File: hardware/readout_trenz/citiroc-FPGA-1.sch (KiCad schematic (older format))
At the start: 17 parts

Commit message: Trenz Module Work in Progress
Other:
- note added: "Replace FPGA with trenz"
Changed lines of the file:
@@
 $Descr A4 11693 8268
 encoding utf-8
-Sheet 11 12
+Sheet 11 13
 Title ""
 Date ""
@@
 	1    0    0    -1
 $EndComp
+Text Notes 4250 1000 0    197  ~ 0
+Replace FPGA with trenz
 $EndSCHEMATC

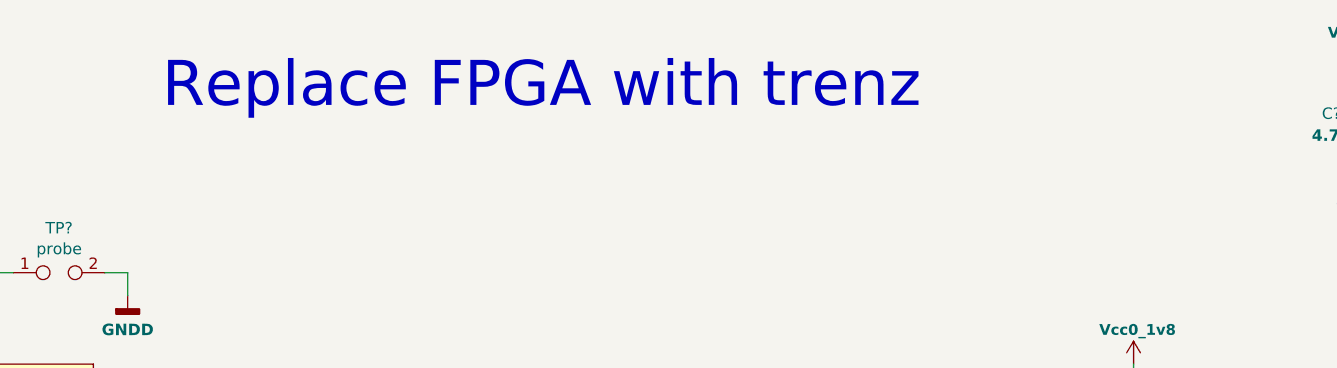
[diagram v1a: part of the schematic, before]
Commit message: Readout Trenz edited
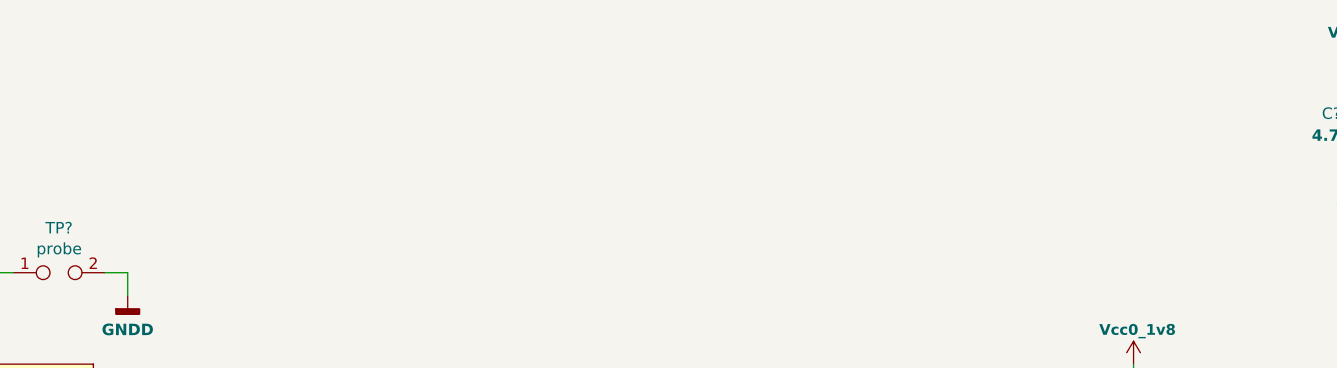
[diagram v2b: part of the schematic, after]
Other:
- note removed: "Replace FPGA with trenz"
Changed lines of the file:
@@
 $Descr A4 11693 8268
 encoding utf-8
-Sheet 11 13
+Sheet 11 20
 Title ""
 Date ""
@@
 AR Path="/605DF89A/606347B4" Ref="U?"  Part="2"
 AR Path="/606347B4" Ref="U?"  Part="2"
+AR Path="/60C32D5A/606347B4" Ref="U?"  Part="2"
 F 0 "U?" H 3375 -2123 50  0000 C CNN
 F 1 "CITIROC1A" H 3375 -2214 50  0000 C CNN
@@
 AR Path="/60548503/606347BA" Ref="U?"  Part="8"
 AR Path="/605DF89A/606347BA" Ref="U?"  Part="8"
+AR Path="/60C32D5A/606347BA" Ref="U?"  Part="8"
 F 0 "U?" H 8175 -1423 50  0000 C CNN
 F 1 "CITIROC1A" H 8175 -1514 50  0000 C CNN
@@
 AR Path="/60548503/606347C0" Ref="C?"  Part="1"
 AR Path="/605DF89A/606347C0" Ref="C?"  Part="1"
+AR Path="/60C32D5A/606347C0" Ref="C?"  Part="1"
 F 0 "C?" H 9842 1096 50  0000 L CNN
 F 1 "47u" H 9800 1000 50  0000 L CNB
@@
 AR Path="/60548503/606347C6" Ref="C?"  Part="1"
 AR Path="/605DF89A/606347C6" Ref="C?"  Part="1"
+AR Path="/60C32D5A/606347C6" Ref="C?"  Part="1"
 F 0 "C?" H 10142 1096 50  0000 L CNN
 F 1 "4.7u" H 10100 1000 50  0000 L CNB
@@
 AR Path="/60548503/606347CC" Ref="C?"  Part="1"
 AR Path="/605DF89A/606347CC" Ref="C?"  Part="1"
+AR Path="/60C32D5A/606347CC" Ref="C?"  Part="1"
 F 0 "C?" H 9592 1096 50  0000 L CNN
 F 1 "4.7u" H 9550 1000 50  0000 L CNB
@@
 AR Path="/60548503/606347D2" Ref="C?"  Part="1"
 AR Path="/605DF89A/606347D2" Ref="C?"  Part="1"
+AR Path="/60C32D5A/606347D2" Ref="C?"  Part="1"
 F 0 "C?" H 11150 1100 50  0000 L CNN
 F 1 ".47u" H 11100 1000 50  0000 L CNB
@@
 AR Path="/60548503/606347D8" Ref="C?"  Part="1"
 AR Path="/605DF89A/606347D8" Ref="C?"  Part="1"
+AR Path="/60C32D5A/606347D8" Ref="C?"  Part="1"
 F 0 "C?" H 10892 1096 50  0000 L CNN
 F 1 ".47u" H 10850 1000 50  0000 L CNB
@@
 AR Path="/60548503/606347DE" Ref="C?"  Part="1"
 AR Path="/605DF89A/606347DE" Ref="C?"  Part="1"
+AR Path="/60C32D5A/606347DE" Ref="C?"  Part="1"
 F 0 "C?" H 10642 1096 50  0000 L CNN
 F 1 ".47u" H 10600 1000 50  0000 L CNB
@@
 AR Path="/60548503/606347E4" Ref="C?"  Part="1"
 AR Path="/605DF89A/606347E4" Ref="C?"  Part="1"
+AR Path="/60C32D5A/606347E4" Ref="C?"  Part="1"
 F 0 "C?" H 10392 1096 50  0000 L CNN
 F 1 ".47u" H 10350 1000 50  0000 L CNB
@@
 AR Path="/60548503/606347EA" Ref="#PWR?"  Part="1"
 AR Path="/605DF89A/606347EA" Ref="#PWR?"  Part="1"
+AR Path="/60C32D5A/606347EA" Ref="#PWR?"  Part="1"
 F 0 "#PWR?" H 9500 1000 50  0001 C CNN
 F 1 "GNDD" H 9500 1100 50  0000 C CNB
@@
 U 1 1 608CECB3
 P 2350 2900
+AR Path="/605DF89A/608CECB3" Ref="R?"  Part="1"
+AR Path="/60C32D5A/608CECB3" Ref="R?"  Part="1"
 F 0 "R?" V 2400 3000 50  0000 L CNN
 F 1 "100" V 2350 2800 50  0000 L CNN
@@
 U 1 1 60D6A41E
 P 3800 1700
+AR Path="/605DF89A/60D6A41E" Ref="TP?"  Part="1"
+AR Path="/60C32D5A/60D6A41E" Ref="TP?"  Part="1"
 F 0 "TP?" H 3800 1895 50  0000 C CNN
 F 1 "probe" H 3800 1804 50  0000 C CNN
@@
 AR Path="/60548503/60D79EC4" Ref="#PWR?"  Part="1"
 AR Path="/605DF89A/60D79EC4" Ref="#PWR?"  Part="1"
+AR Path="/60C32D5A/60D79EC4" Ref="#PWR?"  Part="1"
 F 0 "#PWR?" H 4100 1550 50  0001 C CNN
 F 1 "GNDD" H 4100 1650 50  0000 C CNB
@@
 U 1 1 608D2690
 P 2350 2600
+AR Path="/605DF89A/608D2690" Ref="R?"  Part="1"
+AR Path="/60C32D5A/608D2690" Ref="R?"  Part="1"
 F 0 "R?" V 2400 2700 50  0000 L CNN
 F 1 "100" V 2350 2500 50  0000 L CNN
@@
 U 1 1 60CED0B7
 P 5000 5650
+AR Path="/605DF89A/60CED0B7" Ref="R?"  Part="1"
+AR Path="/60C32D5A/60CED0B7" Ref="R?"  Part="1"
 F 0 "R?" H 5070 5696 50  0000 L CNN
 F 1 "1k" V 5000 5600 50  0000 L CNN
@@
 U 1 1 60CED89A
 P 5100 5650
+AR Path="/605DF89A/60CED89A" Ref="R?"  Part="1"
+AR Path="/60C32D5A/60CED89A" Ref="R?"  Part="1"
 F 0 "R?" H 5170 5696 50  0000 L CNN
 F 1 "1k" V 5100 5600 50  0000 L CNN
@@
 U 1 1 60E0098C
 P 5000 5300
+AR Path="/605DF89A/60E0098C" Ref="U?"  Part="1"
+AR Path="/60C32D5A/60E0098C" Ref="U?"  Part="1"
 F 0 "U?" H 5000 5300 79  0001 C CNN
 F 1 "Vcc0_1v8" H 4850 5350 47  0000 L CNB
@@
 U 1 1 60E0A350
 P 8500 2000
+AR Path="/605DF89A/60E0A350" Ref="U?"  Part="1"
+AR Path="/60C32D5A/60E0A350" Ref="U?"  Part="1"
 F 0 "U?" H 8500 2000 79  0001 C CNN
 F 1 "Vcc0_1v8" H 8350 2050 47  0000 L CNB
@@
 U 1 1 60E13D1D
 P 9500 700
+AR Path="/605DF89A/60E13D1D" Ref="U?"  Part="1"
+AR Path="/60C32D5A/60E13D1D" Ref="U?"  Part="1"
 F 0 "U?" H 9500 700 79  0001 C CNN
 F 1 "Vcc0_1v8" H 9350 750 47  0000 L CNB
@@
 	1    0    0    -1
 $EndComp
-Text Notes 4250 1000 0    197  ~ 0
-Replace FPGA with trenz
 $EndSCHEMATC

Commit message: Readout Trenz in progress
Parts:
- removed C?: .47u, symbol readout_trenz-rescue:C_Small-Device
- removed R? (x2): 100, symbol readout_trenz-rescue:R-Device
- removed R? (x2): 1k, symbol readout_trenz-rescue:R-Device
- removed U? (x3): Vcc0_1v8, symbol readout:VccAux
- added C?: .47u, symbol readout_trenz-rescue:C_Small-Device
- added R? (x2): 100, symbol readout_trenz-rescue:R-Device
- added R? (x2): 1k, symbol readout_trenz-rescue:R-Device
- added U? (x3): Vcc0_1v8, symbol readout:VccAux
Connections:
- net GNDD: now also C?.2
- net NOR32T_oc_1: now also R?.2
- net NOR32_oc_1: now also R?.2
- net Raz_Chn_p1: now also R?.2
- net Raz_chn_n1: now also R?.1
- net VCC: now also C?.1, R?.1, R?.1, U?.1 (VCC), U?.1 (VCC), U?.1 (VCC)
- net Val_Ext_n1: now also R?.1
- net Val_Ext_p1: now also R?.2
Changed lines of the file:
@@
 $Descr A4 11693 8268
 encoding utf-8
-Sheet 11 20
+Sheet 12 20
 Title ""
 Date ""
@@
 $Comp
 L readout_trenz-rescue:C_Small-Device C?
-U 1 1 606347DE
+U 1 1 60C0A1D8
 P 10550 1050
-AR Path="/605605C8/606347DE" Ref="C?"  Part="1"
-AR Path="/60548503/606347DE" Ref="C?"  Part="1"
-AR Path="/605DF89A/606347DE" Ref="C?"  Part="1"
-AR Path="/60C32D5A/606347DE" Ref="C?"  Part="1"
+AR Path="/605605C8/60C0A1D8" Ref="C?"  Part="1"
+AR Path="/60548503/60C0A1D8" Ref="C?"  Part="1"
+AR Path="/605DF89A/60C0A1D8" Ref="C?"  Part="1"
+AR Path="/60C32D5A/60C0A1D8" Ref="C?"  Part="1"
 F 0 "C?" H 10642 1096 50  0000 L CNN
 F 1 ".47u" H 10600 1000 50  0000 L CNB
@@
 AR Path="/605605C8/606347EA" Ref="#PWR?"  Part="1"
 AR Path="/60548503/606347EA" Ref="#PWR?"  Part="1"
-AR Path="/605DF89A/606347EA" Ref="#PWR?"  Part="1"
+AR Path="/605DF89A/606347EA" Ref="#PWR0162"  Part="1"
 AR Path="/60C32D5A/606347EA" Ref="#PWR?"  Part="1"
-F 0 "#PWR?" H 9500 1000 50  0001 C CNN
+F 0 "#PWR0162" H 9500 1000 50  0001 C CNN
 F 1 "GNDD" H 9500 1100 50  0000 C CNB
 F 2 "" H 9500 1250 50  0001 C CNN
@@
 $Comp
 L readout_trenz-rescue:R-Device R?
-U 1 1 608CECB3
+U 1 1 60C0A1DB
 P 2350 2900
-AR Path="/605DF89A/608CECB3" Ref="R?"  Part="1"
-AR Path="/60C32D5A/608CECB3" Ref="R?"  Part="1"
+AR Path="/605DF89A/60C0A1DB" Ref="R?"  Part="1"
+AR Path="/60C32D5A/60C0A1DB" Ref="R?"  Part="1"
 F 0 "R?" V 2400 3000 50  0000 L CNN
 F 1 "100" V 2350 2800 50  0000 L CNN
@@
 AR Path="/605605C8/60D79EC4" Ref="#PWR?"  Part="1"
 AR Path="/60548503/60D79EC4" Ref="#PWR?"  Part="1"
-AR Path="/605DF89A/60D79EC4" Ref="#PWR?"  Part="1"
+AR Path="/605DF89A/60D79EC4" Ref="#PWR0163"  Part="1"
 AR Path="/60C32D5A/60D79EC4" Ref="#PWR?"  Part="1"
-F 0 "#PWR?" H 4100 1550 50  0001 C CNN
+F 0 "#PWR0163" H 4100 1550 50  0001 C CNN
 F 1 "GNDD" H 4100 1650 50  0000 C CNB
 F 2 "" H 4100 1800 50  0001 C CNN
@@
 $Comp
 L readout_trenz-rescue:R-Device R?
-U 1 1 608D2690
+U 1 1 60C0A1DC
 P 2350 2600
-AR Path="/605DF89A/608D2690" Ref="R?"  Part="1"
-AR Path="/60C32D5A/608D2690" Ref="R?"  Part="1"
+AR Path="/605DF89A/60C0A1DC" Ref="R?"  Part="1"
+AR Path="/60C32D5A/60C0A1DC" Ref="R?"  Part="1"
 F 0 "R?" V 2400 2700 50  0000 L CNN
 F 1 "100" V 2350 2500 50  0000 L CNN
@@
 $Comp
 L readout_trenz-rescue:R-Device R?
-U 1 1 60CED0B7
+U 1 1 60C0A1DD
 P 5000 5650
-AR Path="/605DF89A/60CED0B7" Ref="R?"  Part="1"
-AR Path="/60C32D5A/60CED0B7" Ref="R?"  Part="1"
+AR Path="/605DF89A/60C0A1DD" Ref="R?"  Part="1"
+AR Path="/60C32D5A/60C0A1DD" Ref="R?"  Part="1"
 F 0 "R?" H 5070 5696 50  0000 L CNN
 F 1 "1k" V 5000 5600 50  0000 L CNN
@@
 $Comp
 L readout_trenz-rescue:R-Device R?
-U 1 1 60CED89A
+U 1 1 60C0A1DE
 P 5100 5650
-AR Path="/605DF89A/60CED89A" Ref="R?"  Part="1"
-AR Path="/60C32D5A/60CED89A" Ref="R?"  Part="1"
+AR Path="/605DF89A/60C0A1DE" Ref="R?"  Part="1"
+AR Path="/60C32D5A/60C0A1DE" Ref="R?"  Part="1"
 F 0 "R?" H 5170 5696 50  0000 L CNN
 F 1 "1k" V 5100 5600 50  0000 L CNN
@@
 $Comp
 L readout:VccAux U?
-U 1 1 60E0098C
+U 1 1 60C0A1E1
 P 5000 5300
-AR Path="/605DF89A/60E0098C" Ref="U?"  Part="1"
-AR Path="/60C32D5A/60E0098C" Ref="U?"  Part="1"
+AR Path="/605DF89A/60C0A1E1" Ref="U?"  Part="1"
+AR Path="/60C32D5A/60C0A1E1" Ref="U?"  Part="1"
 F 0 "U?" H 5000 5300 79  0001 C CNN
 F 1 "Vcc0_1v8" H 4850 5350 47  0000 L CNB
@@
 $Comp
 L readout:VccAux U?
-U 1 1 60E0A350
+U 1 1 60C0A1E2
 P 8500 2000
-AR Path="/605DF89A/60E0A350" Ref="U?"  Part="1"
-AR Path="/60C32D5A/60E0A350" Ref="U?"  Part="1"
+AR Path="/605DF89A/60C0A1E2" Ref="U?"  Part="1"
+AR Path="/60C32D5A/60C0A1E2" Ref="U?"  Part="1"
 F 0 "U?" H 8500 2000 79  0001 C CNN
 F 1 "Vcc0_1v8" H 8350 2050 47  0000 L CNB
@@
 $Comp
 L readout:VccAux U?
-U 1 1 60E13D1D
+U 1 1 60C0A1E3
 P 9500 700
-AR Path="/605DF89A/60E13D1D" Ref="U?"  Part="1"
-AR Path="/60C32D5A/60E13D1D" Ref="U?"  Part="1"
+AR Path="/605DF89A/60C0A1E3" Ref="U?"  Part="1"
+AR Path="/60C32D5A/60C0A1E3" Ref="U?"  Part="1"
 F 0 "U?" H 9500 700 79  0001 C CNN
 F 1 "Vcc0_1v8" H 9350 750 47  0000 L CNB
